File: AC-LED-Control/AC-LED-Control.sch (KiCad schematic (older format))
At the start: 19 parts, among them P1 CONN_01X02, P2 CONN_01X02, P3 CONN_01X04, SW1 SW_PUSH, U1 STM32F030F4P6, U2 74HC595, U3 74HC595

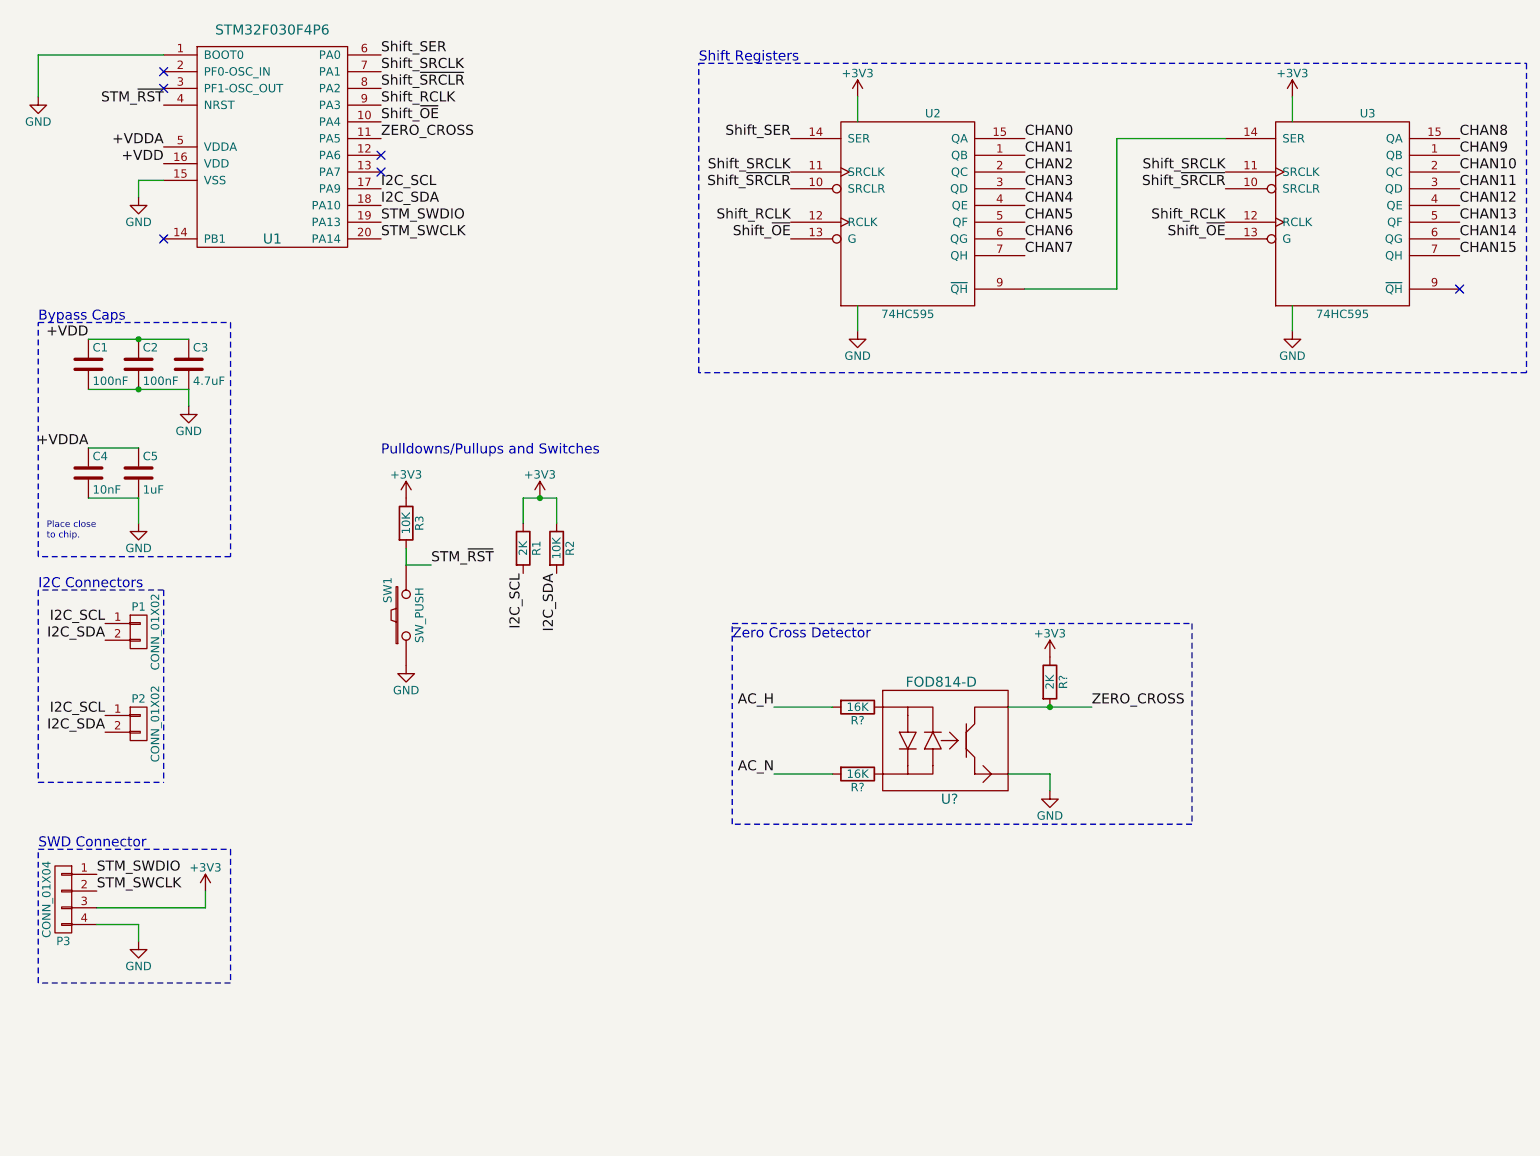
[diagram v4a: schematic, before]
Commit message: Added 16 TRIAC outputs
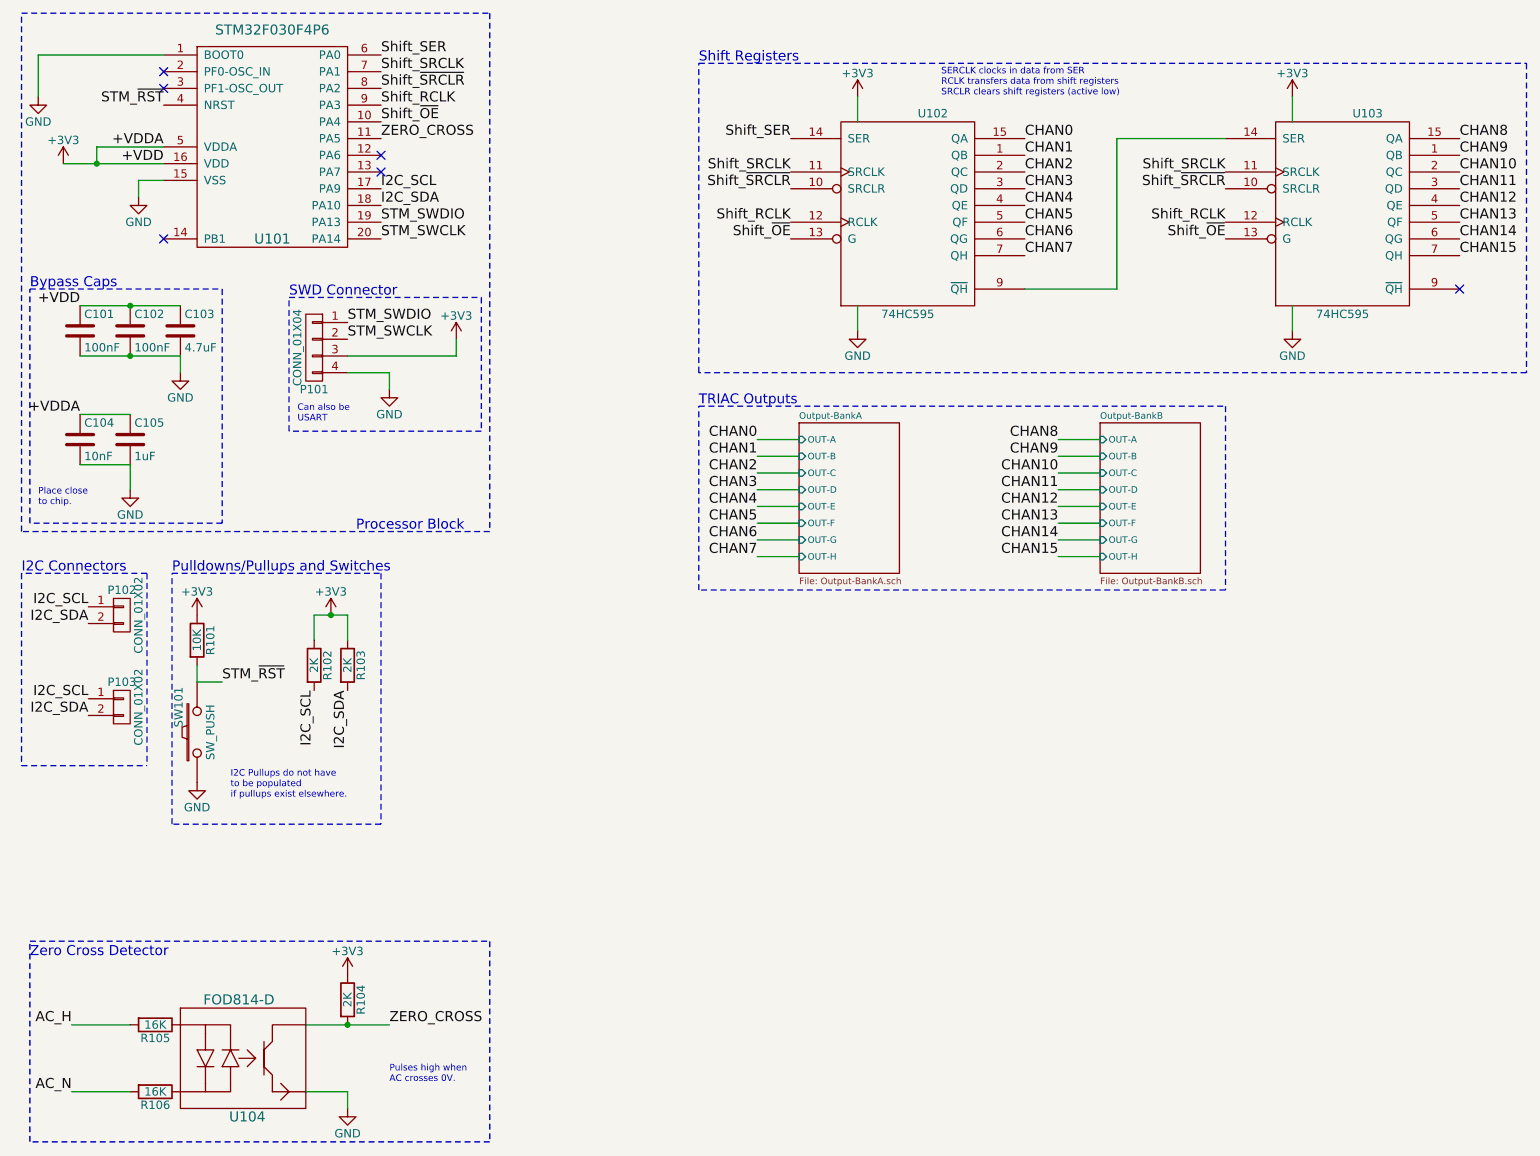
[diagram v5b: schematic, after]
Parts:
- R103: renamed from R2; value 10K -> 2K
- gave numbers to parts that had none: 4
- renumbered C1 to C101, C2 to C102, C3 to C103, C4 to C104, C5 to C105, P3 to P101, P1 to P102, P2 to P103, R3 to R101, R1 to R102, SW1 to SW101, U1 to U101, U2 to U102, U3 to U103
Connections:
- net +VDD is gone; now on net +3V3: C101.1, C102.1, C103.1, U101.16 (VDD)
- net +VDDA is gone; now on net +3V3: C104.1, C105.1, U101.5 (VDDA)
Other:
- note added: "Can also be\nUSART"
- note added: "I2C Pullups do not have \nto be populated\nif pullups exist elsewhere."
- note added: "Processor Block"
- note added: "Pulses high when\nAC crosses 0V."
- note added: "SERCLK clocks in data from SER\nRCLK transfers data from shift registers\nSRCLR clears shift registers (active low)"
- note added: "TRIAC Outputs"
- moved on the sheet: C101, C102, C103, C104, C105, P101, P102, P103, R101, R102, R103, R104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
